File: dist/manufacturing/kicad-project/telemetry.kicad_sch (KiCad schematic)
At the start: 7 parts, among them U29 TMP102AIDRLR, U30 ADS1115IDGSR, U33 SN74LVC1G08DBVR

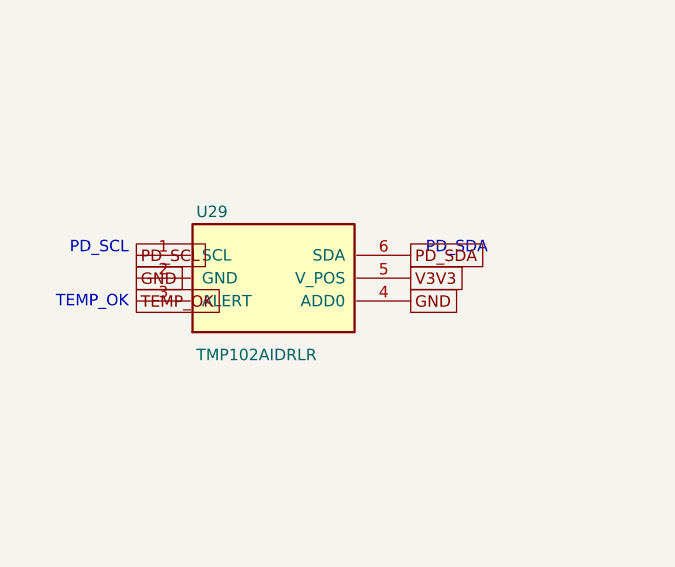
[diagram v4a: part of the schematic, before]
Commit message: Replace unavailable MCU and expander with stocked JLC parts
Use STM32G0B1CEU6 with a grounded UFQFPN48 exposed pad and a 512 KiB
firmware/readback target. Use PCA9538PWR with a PD-powered reset buffer,
bypass capacitor and pulldown to address independent-rail reset injection.

Regenerate local routing, native/manufacturing artifacts, assembly data,
stock evidence and the routed viewer. Preserve unrelated copper and holes
with the existing protected projection. Retain motion locks and physical
qualification holds. Preserve quoted DSN net names and native EP paste sizing.
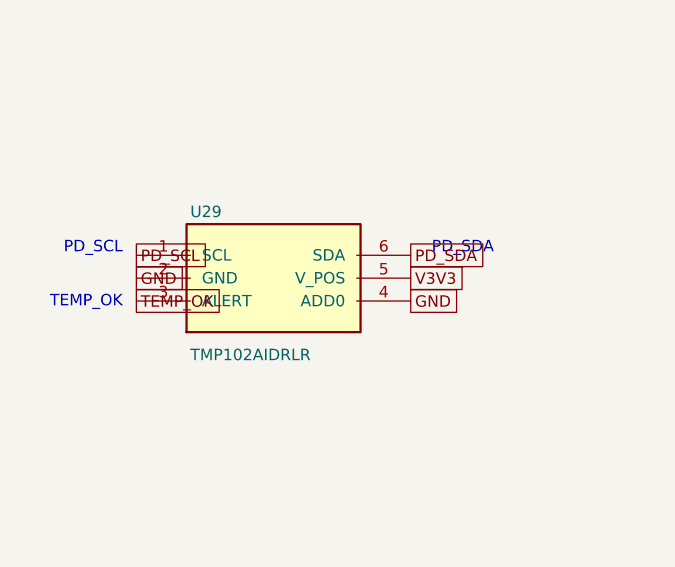
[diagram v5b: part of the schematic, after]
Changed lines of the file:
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@@
     (property "Reference" "U29"
       (id 0)
-      (at 113.33250000000001 81.525 0)
+      (at 112.665 81.525 0)
       (effects
         (font
@@
     (property "Value" "TMP102AIDRLR"
       (id 1)
-      (at 113.33250000000001 97.42499999999998 0)
+      (at 112.665 97.42499999999998 0)
       (effects
         (font
@@
     (instances
       (project ""
-        (path "/857a17cf-af0e-42f8-87e7-32303329b4d2/4c5250fd-354f-4604-98fd-66256cc05fbe"
+        (path "/bf863bdb-065f-43fb-bcd3-832b382d0aae/658db61e-2e51-426b-8244-df4d3e0a4a28"
           (reference "U29")
           (unit 1)
@@
     (instances
       (project ""
-        (path "/857a17cf-af0e-42f8-87e7-32303329b4d2/4c5250fd-354f-4604-98fd-66256cc05fbe"
+        (path "/bf863bdb-065f-43fb-bcd3-832b382d0aae/658db61e-2e51-426b-8244-df4d3e0a4a28"
           (reference "U33")
           (unit 1)
@@
     (instances
       (project ""
-        (path "/857a17cf-af0e-42f8-87e7-32303329b4d2/4c5250fd-354f-4604-98fd-66256cc05fbe"
+        (path "/bf863bdb-065f-43fb-bcd3-832b382d0aae/658db61e-2e51-426b-8244-df4d3e0a4a28"
           (reference "R114")
           (unit 1)
@@
     (instances
       (project ""
-        (path "/857a17cf-af0e-42f8-87e7-32303329b4d2/4c5250fd-354f-4604-98fd-66256cc05fbe"
+        (path "/bf863bdb-065f-43fb-bcd3-832b382d0aae/658db61e-2e51-426b-8244-df4d3e0a4a28"
           (reference "U30")
           (unit 1)
@@
     (instances
       (project ""
-        (path "/857a17cf-af0e-42f8-87e7-32303329b4d2/4c5250fd-354f-4604-98fd-66256cc05fbe"
+        (path "/bf863bdb-065f-43fb-bcd3-832b382d0aae/658db61e-2e51-426b-8244-df4d3e0a4a28"
           (reference "C79")
           (unit 1)
@@
     (instances
       (project ""
-        (path "/857a17cf-af0e-42f8-87e7-32303329b4d2/4c5250fd-354f-4604-98fd-66256cc05fbe"
+        (path "/bf863bdb-065f-43fb-bcd3-832b382d0aae/658db61e-2e51-426b-8244-df4d3e0a4a28"
           (reference "C80")
           (unit 1)
@@
     (instances
       (project ""
-        (path "/857a17cf-af0e-42f8-87e7-32303329b4d2/4c5250fd-354f-4604-98fd-66256cc05fbe"
+        (path "/bf863bdb-065f-43fb-bcd3-832b382d0aae/658db61e-2e51-426b-8244-df4d3e0a4a28"
           (reference "C85")
           (unit 1)
@@
   )
   (text "PD_SCL"
-    (at 105.83250000000001 85.57499999999999 0)
+    (at 105.165 85.57499999999999 0)
     (effects
       (font
@@
   )
   (text "TEMP_OK"
-    (at 105.83250000000001 91.57499999999999 0)
+    (at 105.165 91.57499999999999 0)
     (effects
       (font
@@
   )
   (text "PD_SDA"
-    (at 138.8325 85.57499999999999 0)
-    (effects
-      (font
+    (at 139.5 85.57499999999999 0)
+    (effects
+      (font
